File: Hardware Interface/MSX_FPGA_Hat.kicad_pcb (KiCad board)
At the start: 2 copper layers, 103 x 66 mm, 42 parts, among them J1 J1, J2 J2, J3a1 J3a, J3b1 J3b, J4a1 J4a, J4b1 J4b, J5 Conn_01x03_Female, U1 74LVC245A, U2 74LVC245A, U3 74LVC245A, U4 74LVC245A, U5 74LVC245A, U6 LM1117-3.3

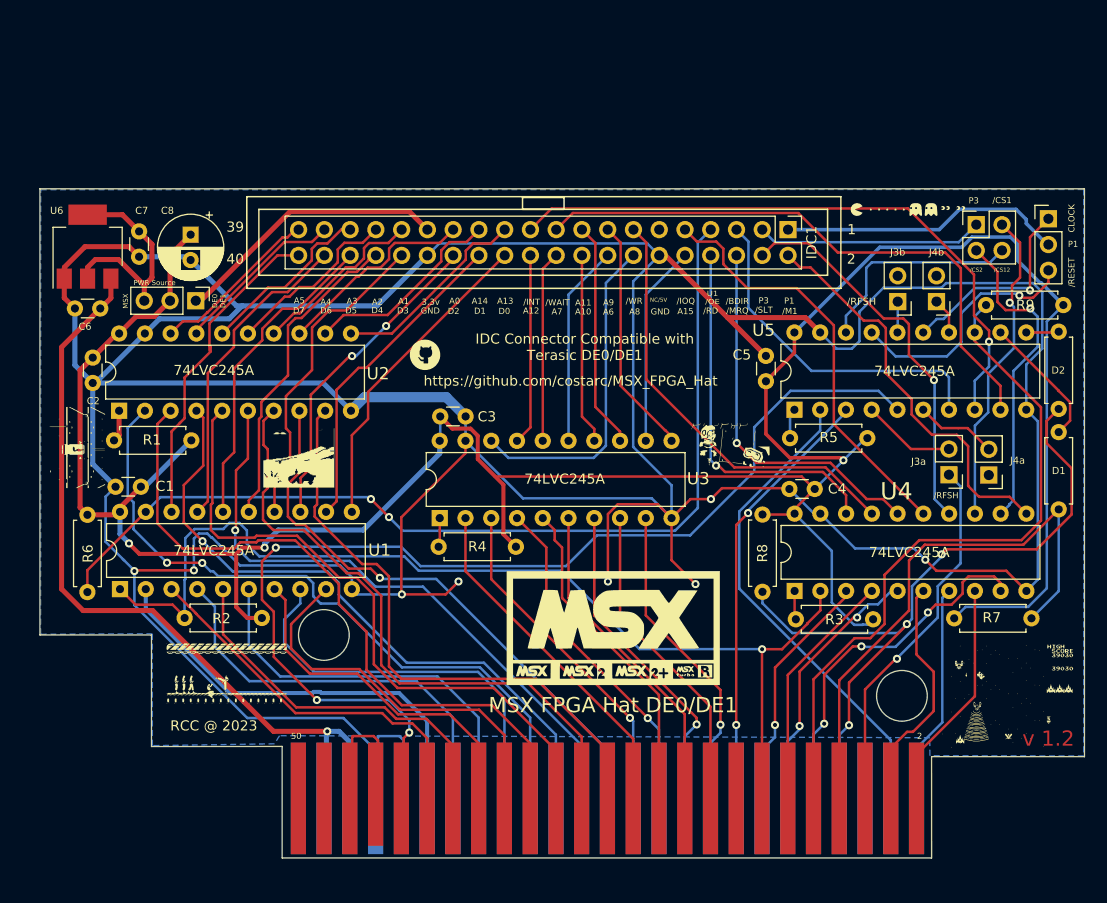
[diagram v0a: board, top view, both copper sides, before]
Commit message: Updated edge connector to meet MSX specifications
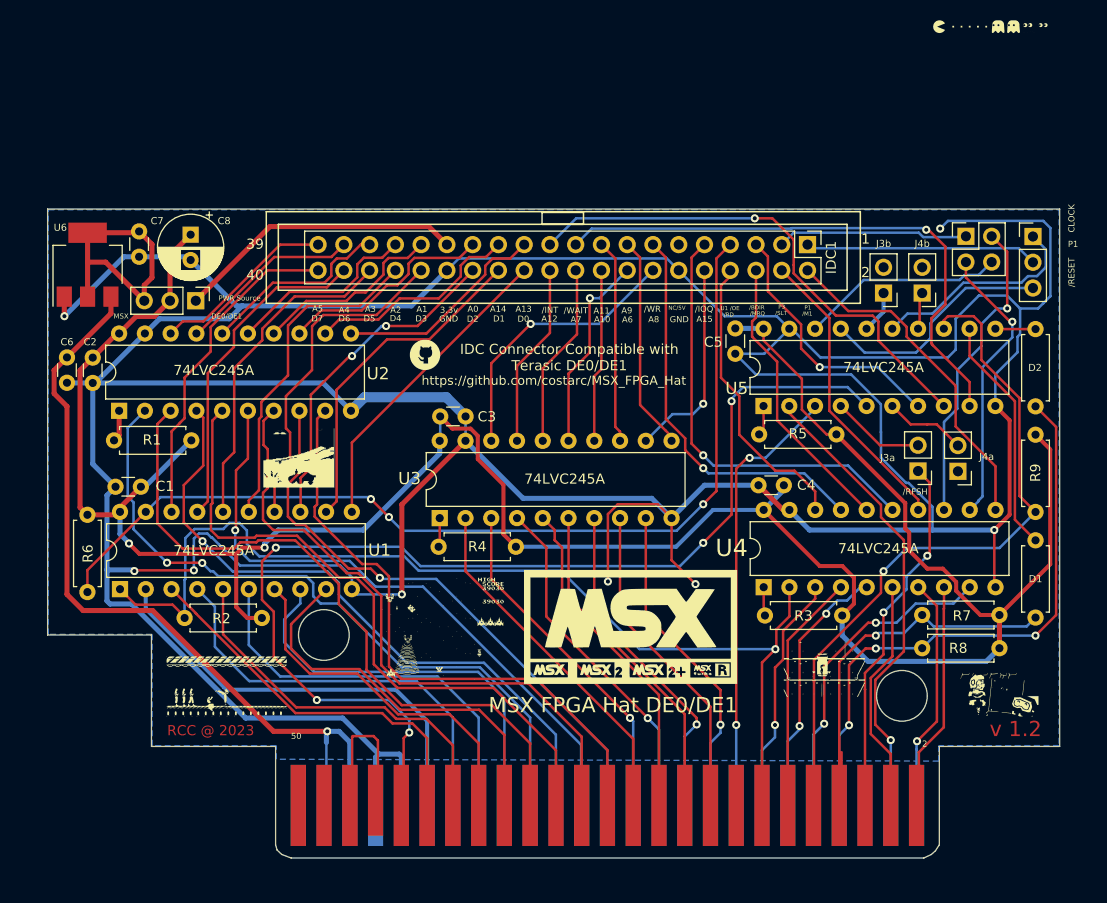
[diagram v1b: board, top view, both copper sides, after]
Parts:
- added G***: LOGO, LOGO, B.Cu at (105.2, 50.8)
- CONN1: footprint Roni Footprints:MSX_CART_SW -> Roni Footprints:MSX_CART_SW_Official
- moved G*** 76.8 mm to (129.3, 67.6), turned to 0 degrees
- moved G*** 56.5 mm to (91.2, 63.8)
- moved G*** 36.2 mm to (146.4, 70.1)
- moved R8 26.8 mm to (146.6, 65.5), turned to 180 degrees
- moved G*** 19.8 mm to (145.8, 4.83)
- moved R9 13.1 mm to (150.1, 44.5), turned to -90 degrees
- moved D1 10.9 mm to (150.1, 62.5)
- moved C6 5.84 mm to (54.6, 36.8), turned to -90 degrees
- moved R7 4.48 mm to (146.6, 62.2), turned to 180 degrees
- moved R5 3.07 mm to (130.5, 44.4)
- moved C4 3.07 mm to (122.8, 49.4)
- moved J3a1 3.07 mm to (138.5, 48.0)
- moved J4a1 3.07 mm to (142.5, 48.1)
- moved R3 3.07 mm to (131.1, 62.3)
- moved U4 3.07 mm to (123.3, 59.5)
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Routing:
- net Vdd: track 268.7 -> 246.0 mm, vias 3 -> 2
- net /INT: track 59.8 -> 40.3 mm, vias 0 -> 1
- net /WAIT: track 71.6 -> 57.4 mm
- net /C_INT: track 61.8 -> 50.6 mm
- net Net-(D1-Pad2): track 13.1 -> 23.6 mm
- net /C_SLTSL: track 38.6 -> 29.2 mm, vias 1 -> 0
- net /C_MREQ: track 37.1 -> 28.5 mm, vias 1 -> 0
- net /C_BUSDIR: track 34.0 -> 26.0 mm, vias 0 -> 1
- net /C_RD: track 36.8 -> 29.0 mm, vias 1 -> 0
- net /C_M1: track 39.9 -> 33.8 mm
- net A6: track 27.6 -> 33.1 mm
- net C_CLK_OR_RST: track 28.1 -> 22.9 mm
- net C_A8: track 32.4 -> 27.4 mm, vias 0 -> 1
- net /M1: track 35.9 -> 31.0 mm, vias 3 -> 2
- net MSX_3.3V: track 21.5 -> 26.3 mm
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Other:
- board size 103 x 66 mm -> 99.8 x 64 mm
- board text added: "DE0/DE1"
- board text removed: "/CS1"
- board text removed: "/CS12"
- board text removed: "/CS2"
- board text removed: "DE0 DE1"
- board text removed: "RCC @ 2023"

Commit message: Finalized v1.3; new silk; new routing for soundin & rfsh; changed jumper J1
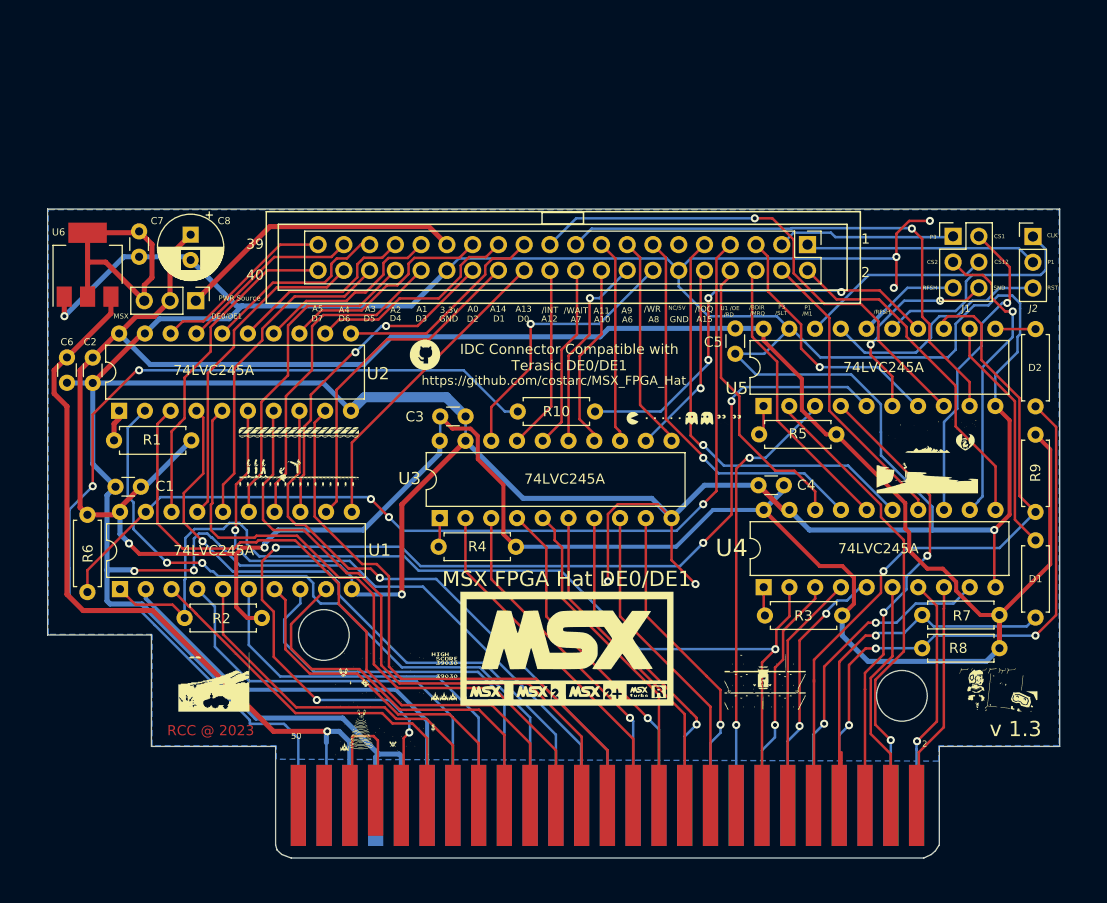
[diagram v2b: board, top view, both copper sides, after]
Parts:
- removed the G*** at (105.2, 50.8)
- removed J3a1: J3a, Connector_PinHeader_2.54mm:PinHeader_1x02_P2.54mm_Vertical
- removed J3b1: J3b, Connector_PinHeader_2.54mm:PinHeader_1x02_P2.54mm_Vertical
- removed J4a1: J4a, Connector_PinHeader_2.54mm:PinHeader_1x02_P2.54mm_Vertical
- removed J4b1: J4b, Connector_PinHeader_2.54mm:PinHeader_1x02_P2.54mm_Vertical
- added G***: LOGO, LOGO, B.Cu at (107.2, 66.0)
- added G***: LOGO, LOGO, B.Cu at (103.1, 36.8)
- added G***: LOGO, LOGO, F.Cu at (139.4, 46.5)
- added R10: 2K2, Resistor_THT:R_Axial_DIN0207_L6.3mm_D2.5mm_P7.62mm_Horizontal, F.Cu at (99.1, 42.2)
- J1: footprint Connector_PinHeader_2.54mm:PinHeader_2x02_P2.54mm_Vertical -> Connector_PinHeader_2.54mm:PinHeader_2x03_P2.54mm_Vertical
- moved G*** 49.0 mm to (115.6, 43.4)
- moved G*** 23.7 mm to (77.5, 46.5)
- moved G*** 23.6 mm to (69.1, 68.8)
- moved G*** 8.67 mm to (86.6, 71.1)
- moved G*** 6.64 mm to (103.9, 65.5)
- moved G*** 5.98 mm to (123.4, 68.8)
- moved J1 1.27 mm to (142.0, 24.9)
- moved G*** 0.50 mm to (146.3, 69.6)
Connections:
- IDC1 pad 11: unconnected-(IDC1-Pad11) -> DE_5V
- U5 pad 16: Net-(J3b1-Pad1) -> /C_RFSH
- U5 pad 4: Net-(J3a1-Pad2) -> /RFSH
- U5 pad 6: Net-(J4a1-Pad2) -> C_SOUNDIN
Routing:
- net SOUNDIN: track 0.00 -> 99.5 mm, vias 0 -> 2
- net Vdd: track 246.0 -> 309.5 mm
- net Net-(U5-Pad14): track 3.68 -> 42.3 mm, vias 0 -> 3
- net C_SOUNDIN: track 0.00 -> 20.5 mm, vias 0 -> 2
- net GNDREF: track 464.4 -> 474.7 mm, vias 8 -> 10
- net /C_RFSH: track 0.00 -> 10.2 mm
- net /RFSH: track 35.4 -> 45.0 mm
- net Net-(J3a1-Pad2): track 9.22 -> 0.00 mm
- net Net-(J4a1-Pad2): track 8.08 -> 0.00 mm
- net Net-(J3b1-Pad1): track 4.21 -> 0.00 mm
- net /C_WAIT: track 55.7 -> 53.7 mm
- net /C_CS2: track 28.2 -> 30.0 mm
- net C_CLOCK: track 21.2 -> 22.5 mm
- net /C_CS_SLT: track 18.9 -> 17.6 mm
- net /C_CS12: track 20.1 -> 18.9 mm
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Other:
- board text added: "CLK"
- board text added: "CS1"
- board text added: "CS12"
- board text added: "CS2"
- board text added: "RFSH"
- board text added: "RST"
- board text added: "SND"
- board text added: "v 1.3"
- board text removed: "/RESET"
- board text removed: "CLOCK"
- board text removed: "v 1.2"

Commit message: Updated footprint for cart with little move in hole places to better fit patola/brazil case
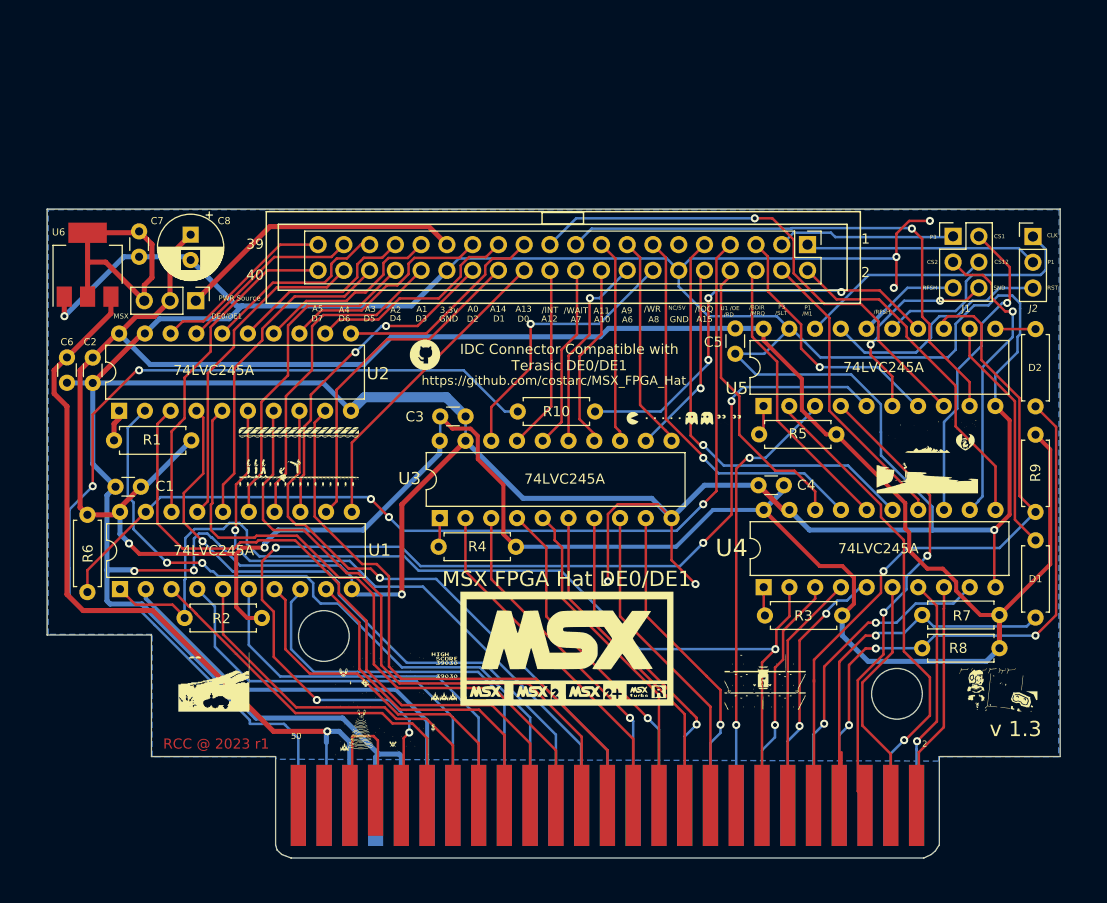
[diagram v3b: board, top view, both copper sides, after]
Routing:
- net D0: track 38.1 -> 32.5 mm
- net /CS12: track 45.2 -> 46.1 mm
- net /SLTSL: track 22.5 -> 23.2 mm
- net /RFSH: track 45.0 -> 45.6 mm
- net D1: track 39.8 -> 39.2 mm
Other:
- board size 99.8 x 64 mm -> 99.9 x 64 mm

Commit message: Added pull-up with 4 x resistor arrays; added reset button
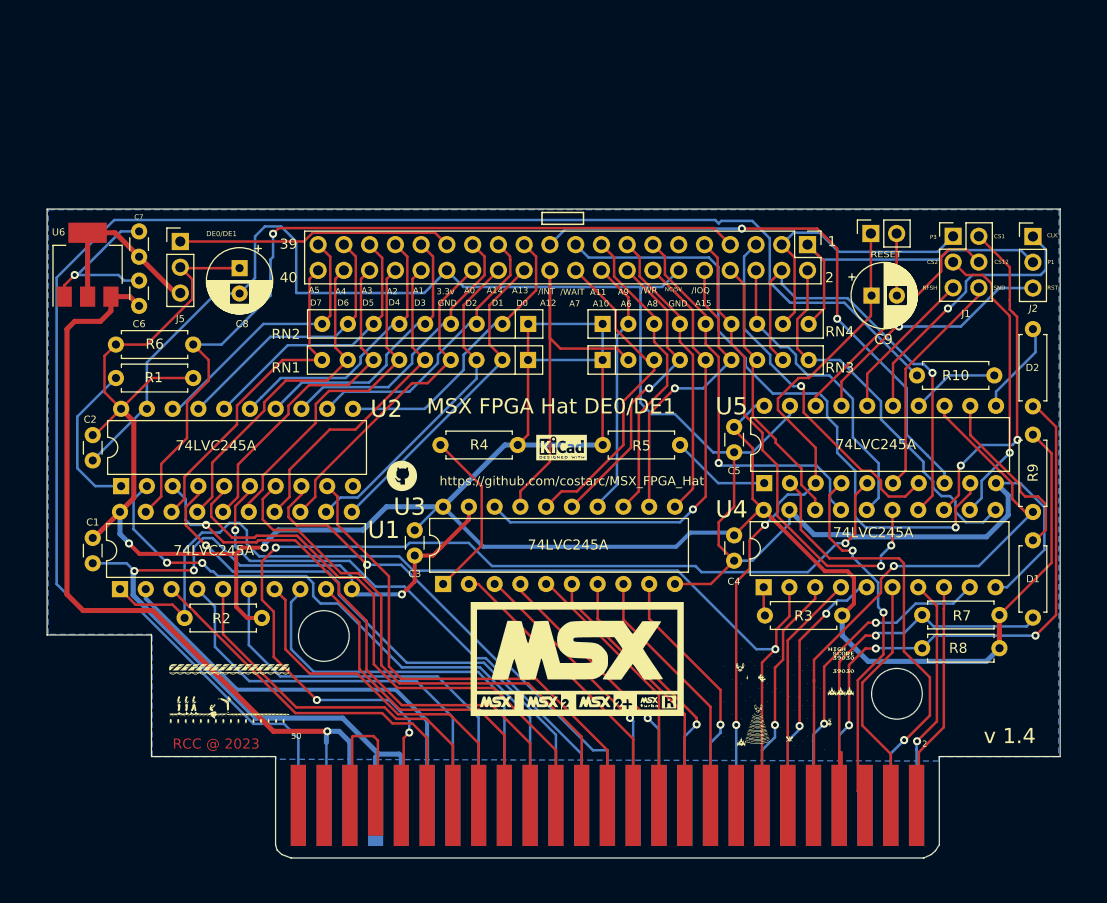
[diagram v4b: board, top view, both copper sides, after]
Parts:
- removed the G*** at (107.2, 66.0)
- removed the G*** at (69.1, 68.8)
- removed the G*** at (139.4, 46.5)
- removed the G*** at (123.4, 68.8)
- added C9: 100uF, Capacitor_THT:CP_Radial_D6.3mm_P2.50mm, F.Cu at (133.9, 30.7)
- added RN1: R_Network10_US, Resistor_THT:R_Array_SIP9, F.Cu at (100.1, 37.1)
- added RN2: R_Network10_US, Resistor_THT:R_Array_SIP9, F.Cu at (100.1, 33.5)
- added RN3: R_Network10_US, Resistor_THT:R_Array_SIP9, F.Cu at (107.4, 37.1)
- added RN4: R_Network10_US, Resistor_THT:R_Array_SIP9, F.Cu at (107.4, 33.5)
- added SW1: SW_Push, Connector_PinSocket_2.54mm:PinSocket_1x02_P2.54mm_Vertical, F.Cu at (133.9, 24.6)
- G***: moved to F.Cu
- G*** (x2): moved to B.Cu
- moved G*** 41.3 mm to (105.2, 65.5), turned to 180 degrees
- moved R10 39.5 mm to (138.4, 38.6)
- moved G*** 39.1 mm to (125.7, 70.6)
- moved G*** 24.4 mm to (70.6, 69.8)
- moved R5 23.1 mm to (107.4, 45.5), turned to 0 degrees
- moved R6 17.0 mm to (59.4, 35.6), turned to 0 degrees
- moved G*** 15.1 mm to (100.7, 40.6), turned to 180 degrees
- moved C3 14.6 mm to (88.9, 56.4), turned to 90 degrees
- moved G*** 12.2 mm to (87.6, 48.5)
- moved R4 10.0 mm to (99.1, 45.5)
- moved C5 9.72 mm to (120.4, 46.2)
- moved G*** 8.89 mm to (103.4, 45.7), turned to 0 degrees
- moved C6 8.74 mm to (61.7, 31.8), turned to 90 degrees
- moved C1 7.87 mm to (57.1, 57.1), turned to 90 degrees
- moved C4 7.82 mm to (120.4, 56.9), turned to 90 degrees
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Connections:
- C6 pad 2: GNDREF -> Net-(C6-Pad2)
- C7 pad 2: GNDREF -> Net-(C6-Pad2)
- U6 pad 1: GNDREF -> Net-(C6-Pad2)
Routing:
- net GNDREF: track 474.7 -> 284.8 mm, vias 10 -> 3
- net SOUNDIN: track 99.5 -> 163.3 mm, vias 2 -> 0
- net Vdd: track 309.5 -> 267.0 mm
- net Net-(R10-Pad2): track 42.3 -> 8.69 mm, vias 3 -> 0
- net /RESET: track 43.0 -> 65.6 mm
- net C_A12: track 18.3 -> 39.8 mm
- net C_A8: track 27.4 -> 47.0 mm
- net Net-(C6-Pad2): track 0.00 -> 17.3 mm, vias 0 -> 1
- net /C_SLTSL: track 29.2 -> 43.8 mm, vias 0 -> 1
- net Net-(R4-Pad2): track 2.87 -> 17.0 mm
- net C_A7: track 18.3 -> 32.3 mm
- net /C_U1_D_OE: track 95.0 -> 81.5 mm, vias 3 -> 1
- net Net-(R1-Pad2): track 3.13 -> 15.5 mm
- net /BUSDIR: track 68.7 -> 57.1 mm
- net A4: track 66.9 -> 55.9 mm, vias 0 -> 1
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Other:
- board text added: "RESET"
- board text added: "v 1.4"
- board text removed: "/BDIR"
- board text removed: "/M1"
- board text removed: "/MRQ"
- board text removed: "/RD"
- board text removed: "/RFSH"
- board text removed: "/SLT"
- board text removed: "MSX"
- board text removed: "PWR Source"
- board text removed: "U1 /OE"
- board text removed: "v 1.3"

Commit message: V 1.5
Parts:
- removed the G*** at (70.6, 69.8)
- removed the G*** at (125.7, 70.6)
- removed the G*** at (103.4, 45.7)
- removed the G*** at (87.6, 48.5)
- removed the G*** at (104.9, 66.5)
- removed the G*** at (100.7, 40.6)
- removed the G*** at (105.2, 65.5)
- added G***: LOGO, LOGO, F.Cu at (104.1, 67.3)
- added RN5: 10K, Resistor_THT:R_Array_SIP9, F.Cu at (75.7, 61.0)
- RN1, RN2, RN3, RN4: value R_Network10_US -> 10K
- U1, U2, U3, U4, U5: value 74LVC245A -> 74LS641-1DW
- moved R2 27.7 mm to (57.3, 40.2), turned to -90 degrees
- moved C1 12.6 mm to (61.5, 45.3), turned to -90 degrees
- moved R6 7.70 mm to (66.9, 37.3)
- moved C2 6.13 mm to (61.6, 42.7)
- moved U2 4.72 mm to (64.4, 47.9)
- moved U1 3.57 mm to (56.7, 57.9)
- moved R1 3.00 mm to (64.5, 37.3)
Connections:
- C6 pad 2: Net-(C6-Pad2) -> GNDREF
- C7 pad 2: Net-(C6-Pad2) -> GNDREF
- R7 pad 1: Vdd -> +5V
- R8 pad 1: Vdd -> +5V
- R9 pad 1: Vdd -> +5V
- U6 pad 1: Net-(C6-Pad2) -> GNDREF
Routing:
- net +5V: track 82.8 -> 190.1 mm, vias 1 -> 3
- net Vdd: track 267.0 -> 194.6 mm, vias 2 -> 0
- net GNDREF: track 284.8 -> 351.5 mm, vias 3 -> 12
- net /C_U1_D_OE: track 81.5 -> 111.5 mm
- net CLOCK: track 101.2 -> 72.2 mm, vias 4 -> 2
- net Net-(C6-Pad2): track 17.3 -> 0.00 mm, vias 1 -> 0
- net D6: track 37.3 -> 50.0 mm, vias 0 -> 1
- net D0: track 32.5 -> 44.8 mm, vias 0 -> 1
- net D2: track 34.7 -> 45.8 mm, vias 0 -> 1
- net D4: track 36.9 -> 46.8 mm, vias 0 -> 1
- net A2: track 56.0 -> 46.5 mm, vias 0 -> 1
- net D7: track 41.3 -> 50.6 mm
- net A0: track 54.2 -> 45.0 mm, vias 0 -> 1
- net D5: track 40.7 -> 48.9 mm
- net A3: track 56.4 -> 48.2 mm, vias 1 -> 0
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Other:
- board text added: "v 1.5"
- board text removed: "/INT"
- board text removed: "/IOQ"
- board text removed: "/WAIT"
- board text removed: "/WR"
- board text removed: "3.3v"
- board text removed: "A0"
- board text removed: "A1"
- board text removed: "A10"
- board text removed: "A11"
- board text removed: "A12"
- board text removed: "A13"
- board text removed: "A14"
- board text removed: "A15"
- board text removed: "A2"
- board text removed: "A3"
- board text removed: "A4"
- board text removed: "A5"
- board text removed: "A6"
- board text removed: "A7"
- board text removed: "A8"
- board text removed: "A9"
- board text removed: "D0"
- board text removed: "D1"
- board text removed: "D2"
- board text removed: "D3"
- board text removed: "D4"
- board text removed: "D5"
- board text removed: "D6"
- board text removed: "D7"
- board text removed: "GND"
- board text removed: "MSX FPGA Hat DE0/DE1"
- board text removed: "NC/5V"
- board text removed: "v 1.4"
